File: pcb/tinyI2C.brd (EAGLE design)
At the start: 84 x 83.2 mm, 37 parts, among them IC1 74LVC1G125DCK, IC2 74LVC1G125DCK, IC3 IC_LDO_MIC5355, U1 LPC824M201JHI33, X1 TSW-112-02-S-S, X2 TSW-112-02-S-S, X3 TSW-106-02-S-S-RA, X4 TSW-102-02-S-S, X5 TSW-102-02-S-S, X6 TSW-102-02-S-S

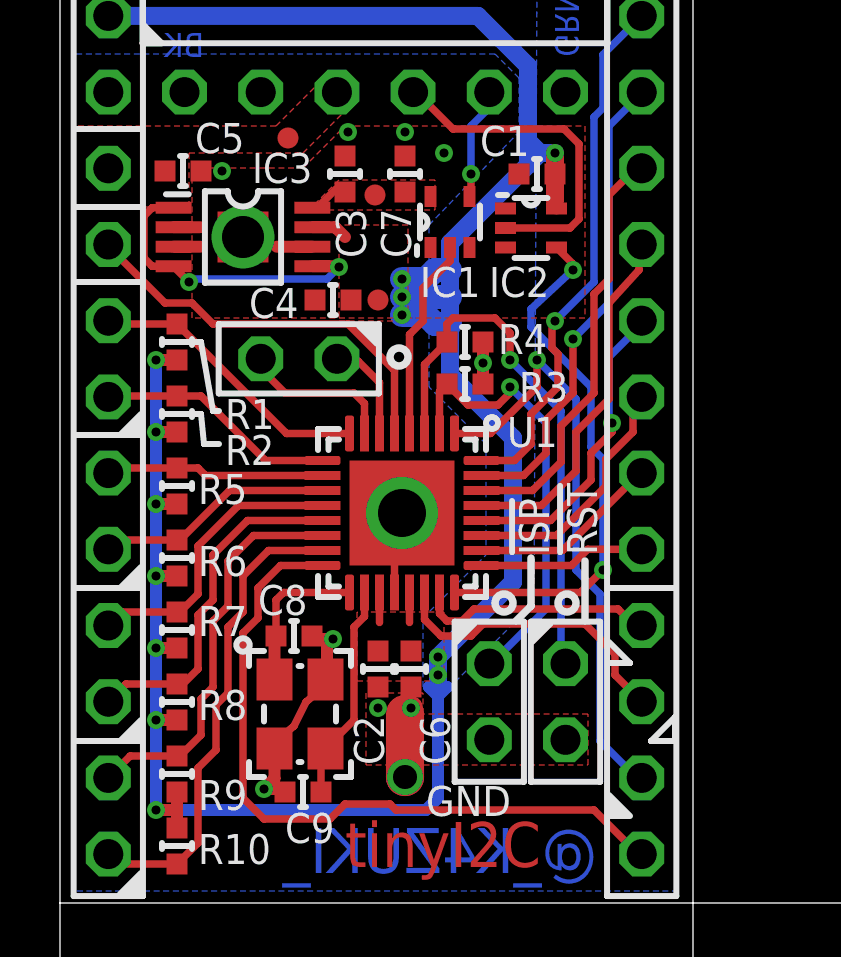
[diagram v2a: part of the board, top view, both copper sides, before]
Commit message: [ PCB ] Q1 silk
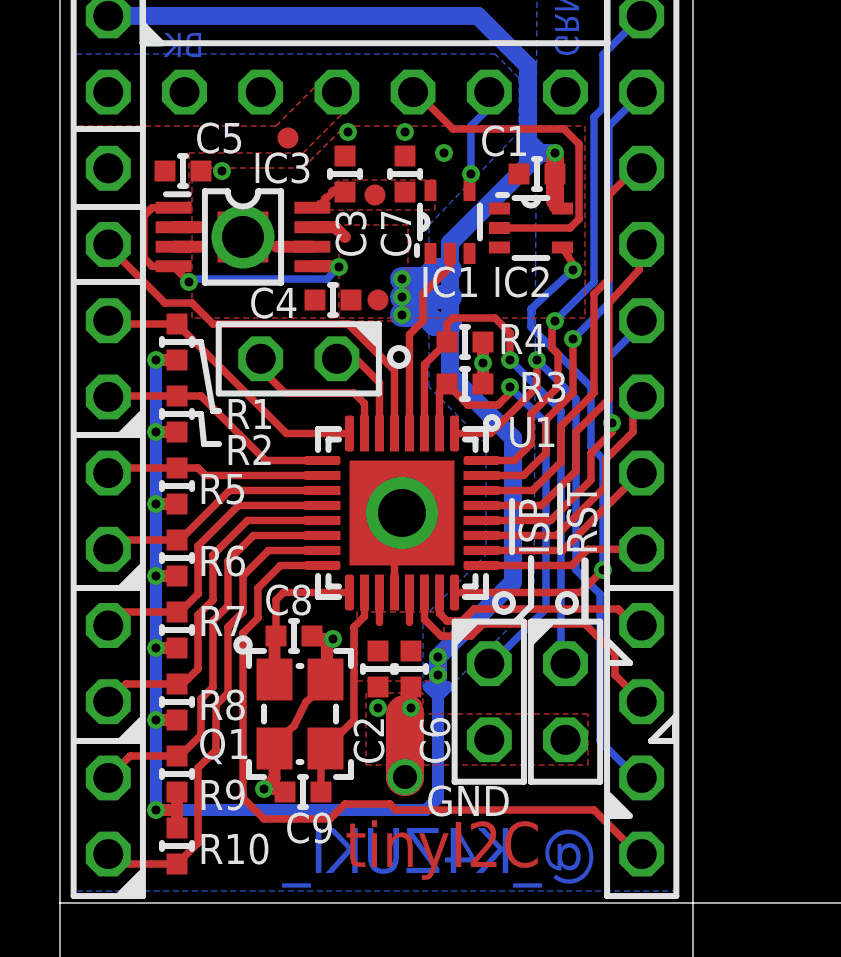
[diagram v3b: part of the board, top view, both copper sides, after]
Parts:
- C1, C2, C6, C7: value 1005 -> 0.1u/1005
- C3, C4, C5: value 1005 -> 10u/1005
- C8, C9: value 1005 -> 18p/1005
- Q1: value (none) -> 12MHz
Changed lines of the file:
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@@
 <text x="4.8" y="38.6" size="0.8" layer="16" font="vector" ratio="20" rot="MR0">BK</text>
 <text x="17.3" y="40.8" size="0.8" layer="16" font="vector" ratio="20" rot="MR270">GRN</text>
-<wire x1="13.4" y1="32.6" x2="13.4" y2="31.9" width="0.1" layer="41"/>
+<wire x1="13.4" y1="32.4" x2="13.4" y2="31.7" width="0.1" layer="41"/>
 <text x="17.9" y="22" size="1" layer="21" font="vector" ratio="20" rot="R90">!RST</text>
 <text x="16.3" y="22" size="1" layer="21" font="vector" ratio="20" rot="R90">!ISP</text>
@@
 <wire x1="10.8" y1="31.1" x2="11.4" y2="31.7" width="0.1" layer="41" curve="-90"/>
 <wire x1="10.8" y1="33" x2="10.8" y2="31.1" width="0.1" layer="41"/>
-<wire x1="12.1" y1="31.8" x2="12.1" y2="32.6" width="0.1" layer="41"/>
-<wire x1="12.6" y1="31.8" x2="12.1" y2="31.8" width="0.2" layer="41"/>
-<wire x1="12.6" y1="31.8" x2="12.6" y2="32.6" width="0.1" layer="41"/>
+<wire x1="12.1" y1="31.6" x2="12.1" y2="32.4" width="0.1" layer="41"/>
+<wire x1="12.6" y1="31.6" x2="12.1" y2="31.6" width="0.2" layer="41"/>
+<wire x1="12.6" y1="31.6" x2="12.6" y2="32.4" width="0.1" layer="41"/>
 <wire x1="4.8" y1="25.7" x2="5.3" y2="25.7" width="0.2" layer="21"/>
 <wire x1="5.1" y1="26.8" x2="5.3" y2="26.8" width="0.2" layer="21"/>
@@
 <wire x1="0" y1="10.8" x2="0.4" y2="10.8" width="0" layer="24"/>
 <text x="12.2" y="13.3" size="1" layer="21" font="vector" ratio="20">GND</text>
-<circle x="11.3" y="28.6" radius="0.3" width="0.25" layer="21"/>
-<circle x="14.8" y="20.4" radius="0.3" width="0.25" layer="21"/>
-<circle x="16.9" y="20.4" radius="0.3" width="0.25" layer="21"/>
-<wire x1="15.7" y1="21.9" x2="15.7" y2="20.3" width="0.25" layer="21"/>
-<wire x1="15.7" y1="20.3" x2="15.2" y2="19.8" width="0.25" layer="21"/>
+<circle x="11.3" y="28.6" radius="0.3" width="0.2" layer="21"/>
+<circle x="14.8" y="20.4" radius="0.3" width="0.2" layer="21"/>
+<circle x="16.9" y="20.4" radius="0.3" width="0.2" layer="21"/>
+<wire x1="15.7" y1="21.9" x2="15.7" y2="20.3" width="0.2" layer="21"/>
+<wire x1="15.7" y1="20.3" x2="15.2" y2="19.8" width="0.2" layer="21"/>
 <wire x1="17.5" y1="21.8" x2="17.5" y2="19.8" width="0.25" layer="21"/>
 <wire x1="16.1" y1="33.9" x2="14.7" y2="32.5" width="0.25" layer="42"/>
@@
 <attribute name="VALUE" x="6.9" y="25.9" size="1.27" layer="27" ratio="10" rot="R270"/>
 </element>
-<element name="C1" library="mylib" package="C0402" value="1005" x="15.9" y="34.7" smashed="yes" rot="R180">
+<element name="C1" library="mylib" package="C0402" value="0.1u/1005" x="15.9" y="34.7" smashed="yes" rot="R180">
 <attribute name="NAME" x="14" y="35.3" size="1" layer="25" font="vector" ratio="20"/>
 <attribute name="VALUE" x="16.535" y="36.605" size="1.27" layer="27" rot="R180"/>
 </element>
-<element name="C2" library="mylib" package="C0402" value="1005" x="10.6" y="18.2" smashed="yes" rot="R270">
+<element name="C2" library="mylib" package="C0402" value="0.1u/1005" x="10.6" y="18.2" smashed="yes" rot="R270">
 <attribute name="NAME" x="10.8" y="15" size="1" layer="25" font="vector" ratio="20" rot="R90"/>
 <attribute name="VALUE" x="8.695" y="18.835" size="1.27" layer="27" rot="R270"/>
 </element>
-<element name="C4" library="mylib" package="C0402" value="1005" x="9.1" y="30.5" smashed="yes" rot="R180">
+<element name="C4" library="mylib" package="C0402" value="10u/1005" x="9.1" y="30.5" smashed="yes" rot="R180">
 <attribute name="NAME" x="6.3" y="29.9" size="1" layer="25" font="vector" ratio="20"/>
 <attribute name="VALUE" x="9.735" y="32.405" size="1.27" layer="27" rot="R180"/>
 </element>
-<element name="C5" library="mylib" package="C0402" value="1005" x="4.1" y="34.8" smashed="yes">
+<element name="C5" library="mylib" package="C0402" value="10u/1005" x="4.1" y="34.8" smashed="yes">
 <attribute name="NAME" x="4.5" y="35.4" size="1" layer="25" font="vector" ratio="20"/>
 <attribute name="VALUE" x="3.465" y="32.895" size="1.27" layer="27"/>
@@
 <attribute name="VALUE" x="5.805" y="11.665" size="1.27" layer="27" rot="R90"/>
 </element>
-<element name="C3" library="mylib" package="C0402" value="1005" x="9.5" y="34.7" smashed="yes" rot="R90">
+<element name="C3" library="mylib" package="C0402" value="10u/1005" x="9.5" y="34.7" smashed="yes" rot="R90">
 <attribute name="NAME" x="10.2" y="31.9" size="1" layer="25" font="vector" ratio="20" rot="R90"/>
 <attribute name="VALUE" x="11.405" y="34.065" size="1.27" layer="27" rot="R90"/>
@@
 <attribute name="VALUE" x="20.66" y="43.145" size="1.27" layer="27" rot="R180"/>
 </element>
-<element name="C6" library="mylib" package="C0402" value="1005" x="11.7" y="18.2" smashed="yes" rot="R270">
+<element name="C6" library="mylib" package="C0402" value="0.1u/1005" x="11.7" y="18.2" smashed="yes" rot="R270">
 <attribute name="NAME" x="13" y="15" size="1" layer="25" font="vector" ratio="20" rot="R90"/>
 <attribute name="VALUE" x="9.795" y="18.835" size="1.27" layer="27" rot="R270"/>
@@
 </element>
 <element name="IC2" library="74xx-little-us_local" package="SC70-5" value="74LVC1G125DCK" x="15.7" y="32.9" smashed="yes" rot="R270">
-<attribute name="NAME" x="14.3" y="30.6" size="1" layer="25" font="vector" ratio="20"/>
+<attribute name="NAME" x="14.4" y="30.6" size="1" layer="25" font="vector" ratio="20"/>
 <attribute name="VALUE" x="13.16" y="35.44" size="1.27" layer="27" rot="R270"/>
 </element>
-<element name="C7" library="mylib" package="C0402" value="1005" x="11.5" y="34.7" smashed="yes" rot="R90">
+<element name="C7" library="mylib" package="C0402" value="0.1u/1005" x="11.5" y="34.7" smashed="yes" rot="R90">
 <attribute name="NAME" x="11.7" y="31.9" size="1" layer="25" font="vector" ratio="20" rot="R90"/>
 <attribute name="VALUE" x="13.405" y="34.065" size="1.27" layer="27" rot="R90"/>
@@
 <attribute name="VALUE" x="3.56" y="29.298" size="1.27" layer="27" ratio="10"/>
 </element>
-<element name="Q1" library="adafruit (1)" package="NX3225" value="" x="8" y="16.7" rot="R270"/>
-<element name="C8" library="mylib" package="C0402" value="1005" x="7.8" y="19.3" smashed="yes">
-<attribute name="NAME" x="6.6" y="20" size="1" layer="25" font="vector" ratio="20"/>
+<element name="Q1" library="adafruit (1)" package="NX3225" value="12MHz" x="8" y="16.7" smashed="yes" rot="R270">
+<attribute name="NAME" x="4.6" y="15.2" size="1" layer="25" font="vector" ratio="20"/>
+</element>
+<element name="C8" library="mylib" package="C0402" value="18p/1005" x="7.8" y="19.3" smashed="yes">
+<attribute name="NAME" x="6.8" y="20" size="1" layer="25" font="vector" ratio="20"/>
 <attribute name="VALUE" x="7.165" y="17.395" size="1.27" layer="27"/>
 </element>
-<element name="C9" library="mylib" package="C0402" value="1005" x="8.1" y="14.1" smashed="yes" rot="R180">
+<element name="C9" library="mylib" package="C0402" value="18p/1005" x="8.1" y="14.1" smashed="yes" rot="R180">
 <attribute name="NAME" x="7.5" y="12.4" size="1" layer="25" font="vector" ratio="20"/>
 <attribute name="VALUE" x="8.735" y="16.005" size="1.27" layer="27" rot="R180"/>
@@
 <wire x1="17.3" y1="35.7" x2="17.3" y2="33.2" width="0.25" layer="1"/>
 <wire x1="17.3" y1="33.2" x2="17" y2="32.9" width="0.25" layer="1"/>
-<wire x1="17" y1="32.9" x2="14.85" y2="32.9" width="0.25" layer="1"/>
+<wire x1="17" y1="32.9" x2="14.65" y2="32.9" width="0.25" layer="1"/>
 </signal>
 <signal name="RX&lt;-">
@@
 <wire x1="14.31" y1="36.91" x2="13.7" y2="36.3" width="0.25" layer="16"/>
 <wire x1="13.7" y1="36.3" x2="13.7" y2="34.7" width="0.25" layer="16"/>
-<wire x1="13.65" y1="33.95" x2="13.7" y2="34" width="0.25" layer="1"/>
+<wire x1="13.65" y1="34.15" x2="13.7" y2="34" width="0.25" layer="1"/>
 <wire x1="13.7" y1="34" x2="13.7" y2="34.7" width="0.25" layer="1"/>
 </signal>
@@
 <wire x1="13" y1="28" x2="15.1" y2="25.9" width="0.6" layer="16"/>
 <wire x1="15.1" y1="21.1" x2="12.6" y2="18.6" width="0.6" layer="16"/>
-<wire x1="16.5" y1="33.6" x2="16.55" y2="33.55" width="0.4" layer="1"/>
+<wire x1="16.5" y1="33.6" x2="16.75" y2="33.55" width="0.4" layer="1"/>
 <wire x1="16.5" y1="33.6" x2="16.5" y2="33.8" width="0.4" layer="1"/>
 <wire x1="16.5" y1="33.8" x2="16.5" y2="34.7" width="0.6" layer="1"/>
@@
 <contactref element="IC1" pad="2"/>
 <wire x1="11.65" y1="29.35" x2="12.1" y2="29.8" width="0.25" layer="1"/>
-<wire x1="13" y1="32.25" x2="13" y2="31.8" width="0.25" layer="1"/>
-<wire x1="13" y1="31.8" x2="12.1" y2="30.9" width="0.25" layer="1"/>
-<wire x1="12.1" y1="30.9" x2="12.1" y2="29.8" width="0.25" layer="1"/>
+<wire x1="13" y1="32.05" x2="13" y2="31.6" width="0.25" layer="1"/>
+<wire x1="13" y1="31.6" x2="12.1" y2="30.7" width="0.25" layer="1"/>
+<wire x1="12.1" y1="30.7" x2="12.1" y2="29.8" width="0.25" layer="1"/>
 </signal>
 <signal name="TGT_RX">
@@
 <via x="17.1" y="31.5" extent="1-16" drill="0.3"/>
 <wire x1="17.1" y1="31.5" x2="17.1" y2="31.7" width="0.25" layer="1"/>
-<wire x1="17.1" y1="31.7" x2="16.55" y2="32.25" width="0.25" layer="1"/>
+<wire x1="17.1" y1="31.7" x2="16.75" y2="32.25" width="0.25" layer="1"/>
 </signal>
 <signal name="!ISP!">

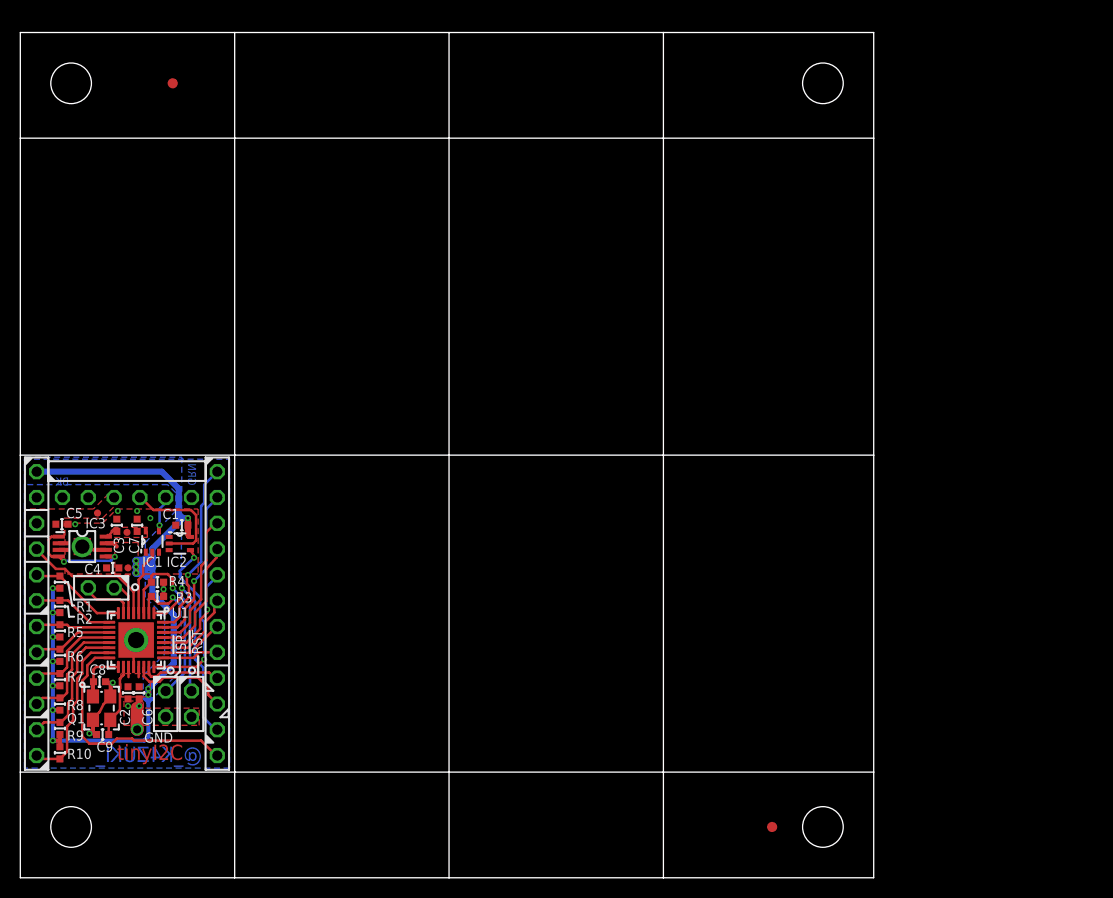
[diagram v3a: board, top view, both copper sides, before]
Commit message: [ PCB ] add minlab icon;panel fix
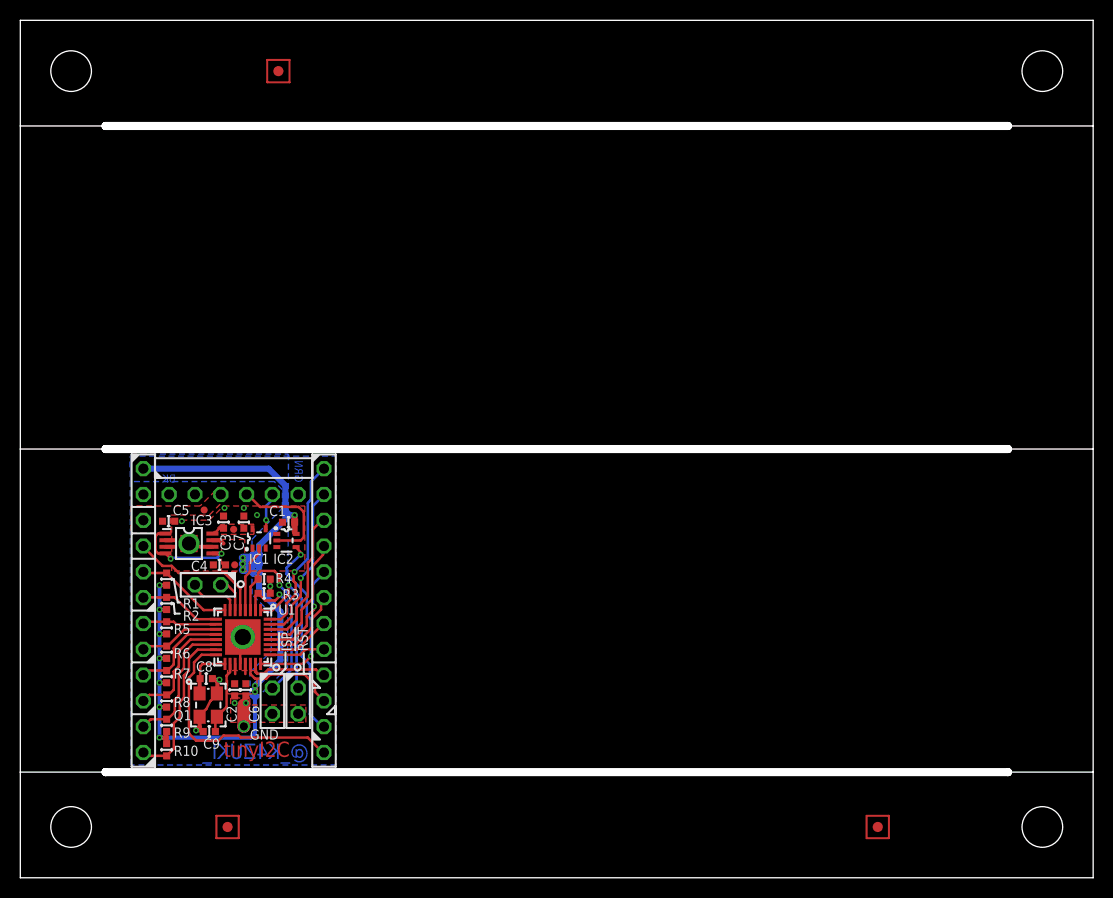
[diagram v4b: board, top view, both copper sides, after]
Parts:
- added I1: ICON_MINLAB_5.2S, mylib:ICON_MINLAB_5.2MM
- added TP8: TPTP10R, testpad:TP10R
- moved C2 10.5 mm to (21.1, 18.5)
- moved C4 10.5 mm to (19.6, 30.8)
- moved C9 10.5 mm to (18.6, 14.4)
- moved IC3 10.5 mm to (16.6, 32.9)
- moved TP1 10.5 mm to (18.1, 36.2)
- moved TP2 10.5 mm to (21.1, 30.8)
- moved C3 10.5 mm to (20.0, 35.0)
- moved C5 10.5 mm to (14.6, 35.1)
- moved C6 10.5 mm to (22.2, 18.5)
- moved C7 10.5 mm to (22.0, 35.0)
- moved C8 10.5 mm to (18.3, 19.6)
- moved IC1 10.5 mm to (23.5, 33.4)
- moved IC2 10.5 mm to (26.2, 33.2)
- moved Q1 10.5 mm to (18.5, 17.0)
- moved R1 10.5 mm to (14.4, 29.4)
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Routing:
- net N$5: track 0.00 -> 8.80 mm
- net N$4: track 0.00 -> 8.80 mm
- net N$2: track 0.00 -> 8.80 mm
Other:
- board size 84 x 83.2 mm -> 105.6 x 84.4 mm

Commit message: [ PCB ] library update
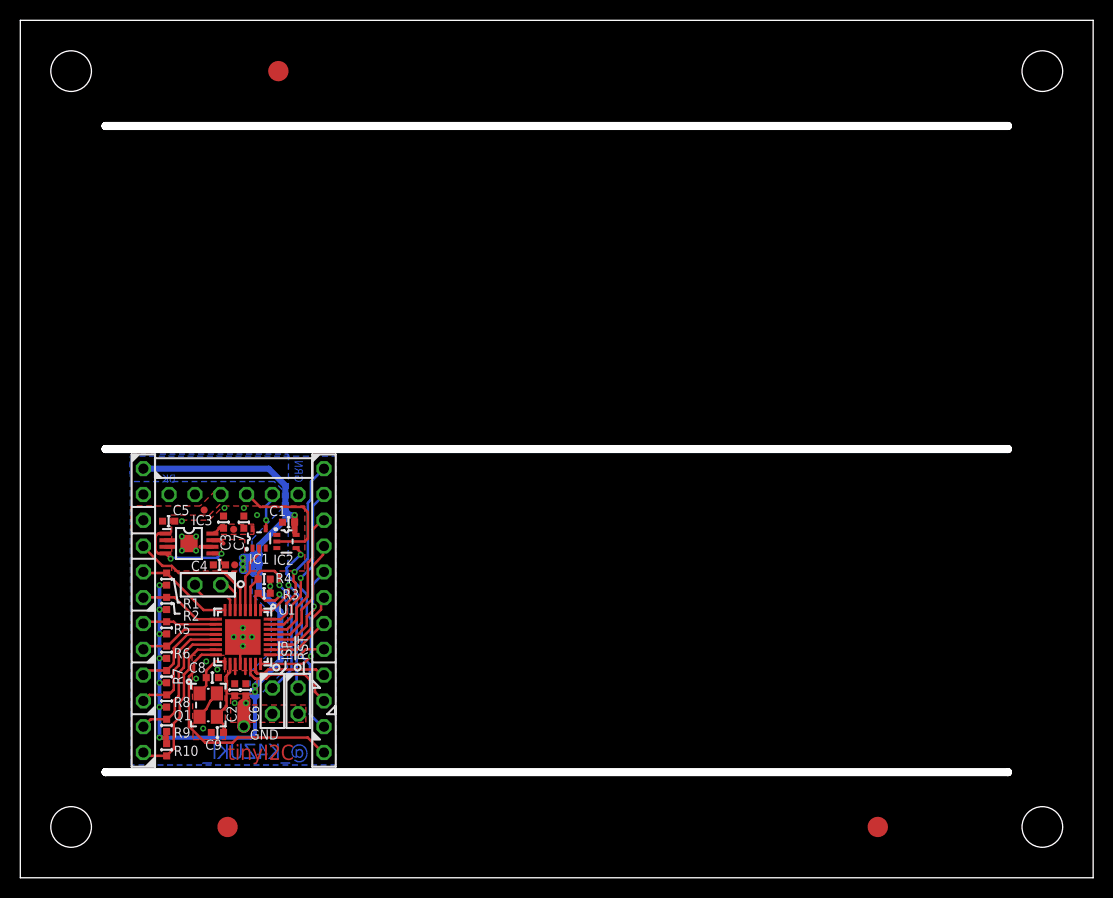
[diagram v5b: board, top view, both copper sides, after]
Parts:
- IC3: device mylib:IC_08_0.65_160MIL -> mylib:IC_08_0.65_160MIL_EP
- TP4, TP5, TP8: value TPTP10R -> TPTP20R; device testpad:TP10R -> testpad_local:TP20R
- moved I1 2.40 mm to (20.0, 22.5), turned to 0 degrees
- moved C9 0.81 mm to (19.4, 14.3)
- moved C8 0.61 mm to (18.9, 19.7)
- moved IC2 0.10 mm to (26.2, 33.1)
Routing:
- net N$5: track 8.80 -> 0.00 mm
- net N$4: track 8.80 -> 0.00 mm
- net N$2: track 8.80 -> 0.00 mm
- net GND: track 15.6 -> 11.2 mm, vias 11 -> 20
- net TX->: track 11.6 -> 12.5 mm
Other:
- outline, holes or cut-outs redrawn
